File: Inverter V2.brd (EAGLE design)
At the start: 194.6 x 115.3 mm, 30 parts, among them Q1 ROHM_SCT3022ALGC11ROHM_SCT302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, Q2 ROHM_SCT3022ALGC11ROHM_SCT302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, Q3 ROHM_SCT3022ALGC11ROHM_SCT302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, Q4 ROHM_SCT3022ALGC11ROHM_SCT302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, Q5 ROHM_SCT3022ALGC11ROHM_SCT302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, Q6 ROHM_SCT3022ALGC11ROHM_SCT302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, U1 RASPBERRY_PICOTH

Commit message: Routing Inverter V2
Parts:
- added A0, A1: (no value), microbuilder:SOLDERJUMPER_REFLOW_NOPASTE
- added C4: 0.1µF, microbuilder:0603-NO
- added R12: 10K, microbuilder:RESPACK_4X0603
- added U2: INA219BIDCNT, microbuilder:SOT23-8
- SHUNT: device SparkFun-Connectors:1X02_2.54_SCREWTERM -> SparkFun-Connectors:1X02_XTRA_BIG
- VOUT: device SparkFun-Connectors:SCREWTERMINAL-3.5MM-3_LOCK.007S -> SparkFun-Connectors:SCREWTERMINAL-3.5MM-3-NS
- moved R8 127.0 mm to (31.3, 49.8), turned to 270 degrees
- moved R10 76.4 mm to (82.1, 53.6)
- moved R7 75.8 mm to (82.7, 76.3)
- moved R1 55.0 mm to (143.9, 20.1), turned to 90 degrees
- moved R6 23.6 mm to (62.6, 78.5)
- moved R11 16.9 mm to (66.2, 38.6)
- moved SHUNT 12.8 mm to (178.0, 52.5), turned to 90 degrees
- moved R9 12.1 mm to (68.4, 66.5)
- moved V+ 11.2 mm to (120.8, 16.1)
- moved C3 8.69 mm to (37.2, 56.3), turned to 180 degrees
- moved VOUT 7.08 mm to (188.3, 67.6)
- moved C7 7.01 mm to (57.7, 56.2)
- moved C6 6.98 mm to (53.3, 57.5)
- moved Q2 4.61 mm to (82.5, 64.9)
- moved Q6 4.61 mm to (164.0, 42.0)
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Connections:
- net N$1 renamed HIN1
- net N$10 renamed VGIN3
- net N$11 renamed VGIN2
- net N$12 renamed HO3
- net N$14 renamed VGIN6
- net N$16 renamed VGIN4
- net N$2 renamed LO1
- net N$3 renamed LIN1
- net N$5 renamed LIN2
- net N$6 renamed VGIN1
- net N$7 renamed HIN3
- net N$8 renamed VGIN5
- net N$9 renamed LIN3
- removed net VBUS: U1.40
- new net ADDR0: A0.2, R12.5, U2.7
- new net ADDR1: A1.2, R12.6, U2.8
- new net SCL: U1.2, U2.5
- new net SDA: U1.1, U2.6
- new net VCC: A0.1, A1.1, C4.1, U1.40, U2.4
- net GND1: now also C4.2, R12.3, R12.4, SHUNT.1, U2.2, U2.3; no longer SHUNT.P1
- net SHUNT: now also SHUNT.2, U2.1; no longer SHUNT.P2
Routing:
- net SHUNT: track 0.00 -> 246.4 mm
- net VOUT3/VS3: track 0.00 -> 189.3 mm
- net VS1/VOUT1: track 0.00 -> 166.3 mm
- net V+: track 0.00 -> 153.6 mm, vias 0 -> 2
- net VS2/VOUT2: track 0.00 -> 144.2 mm, vias 0 -> 2
- net VGIN6: track 0.00 -> 142.9 mm
- net VCC: track 0.00 -> 106.4 mm
- net VGIN5: track 0.00 -> 83.6 mm
- net VGIN4: track 0.00 -> 83.2 mm
- net SDA: track 0.00 -> 80.6 mm
- net VDD: track 0.00 -> 80.0 mm, vias 0 -> 2
- net SCL: track 0.00 -> 72.1 mm
- net VB3: track 0.00 -> 56.9 mm, vias 0 -> 2
- net LO1: track 0.00 -> 36.7 mm
- net LO2: track 0.00 -> 35.7 mm
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- added copper zone on layer 1, net GND1
- removed copper zone on layer 16, net GND1
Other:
- board size 194.6 x 115.3 mm -> 193.8 x 114 mm

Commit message: Revision to routed V2 inverter
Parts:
- C7: device rcl:SMC_Z -> rcl:E5-5
- moved C7 73.1 mm to (122.0, 21.5), turned to 0 degrees
- moved R11 18.5 mm to (51.7, 50.1), turned to 315 degrees
- moved R9 1.12 mm to (69.5, 66.5), turned to 45 degrees
- moved R6 0.90 mm to (63.4, 78.2), turned to 45 degrees
- moved C6 0.84 mm to (54.1, 57.5), turned to 315 degrees
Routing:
- net V+: track 153.6 -> 131.9 mm, vias 2 -> 0
- net HO3: track 34.9 -> 15.6 mm
- net VCC: track 106.4 -> 123.2 mm, vias 0 -> 2
- net VGIN3: track 19.0 -> 30.9 mm
- net GND1: track 1.25 -> 7.87 mm, vias 0 -> 2
- net VGIN1: track 27.0 -> 24.7 mm, vias 2 -> 1
- net VGIN2: track 14.7 -> 13.5 mm
- net HO1: track 18.3 -> 17.5 mm
- net N$15: track 4.21 -> 3.55 mm

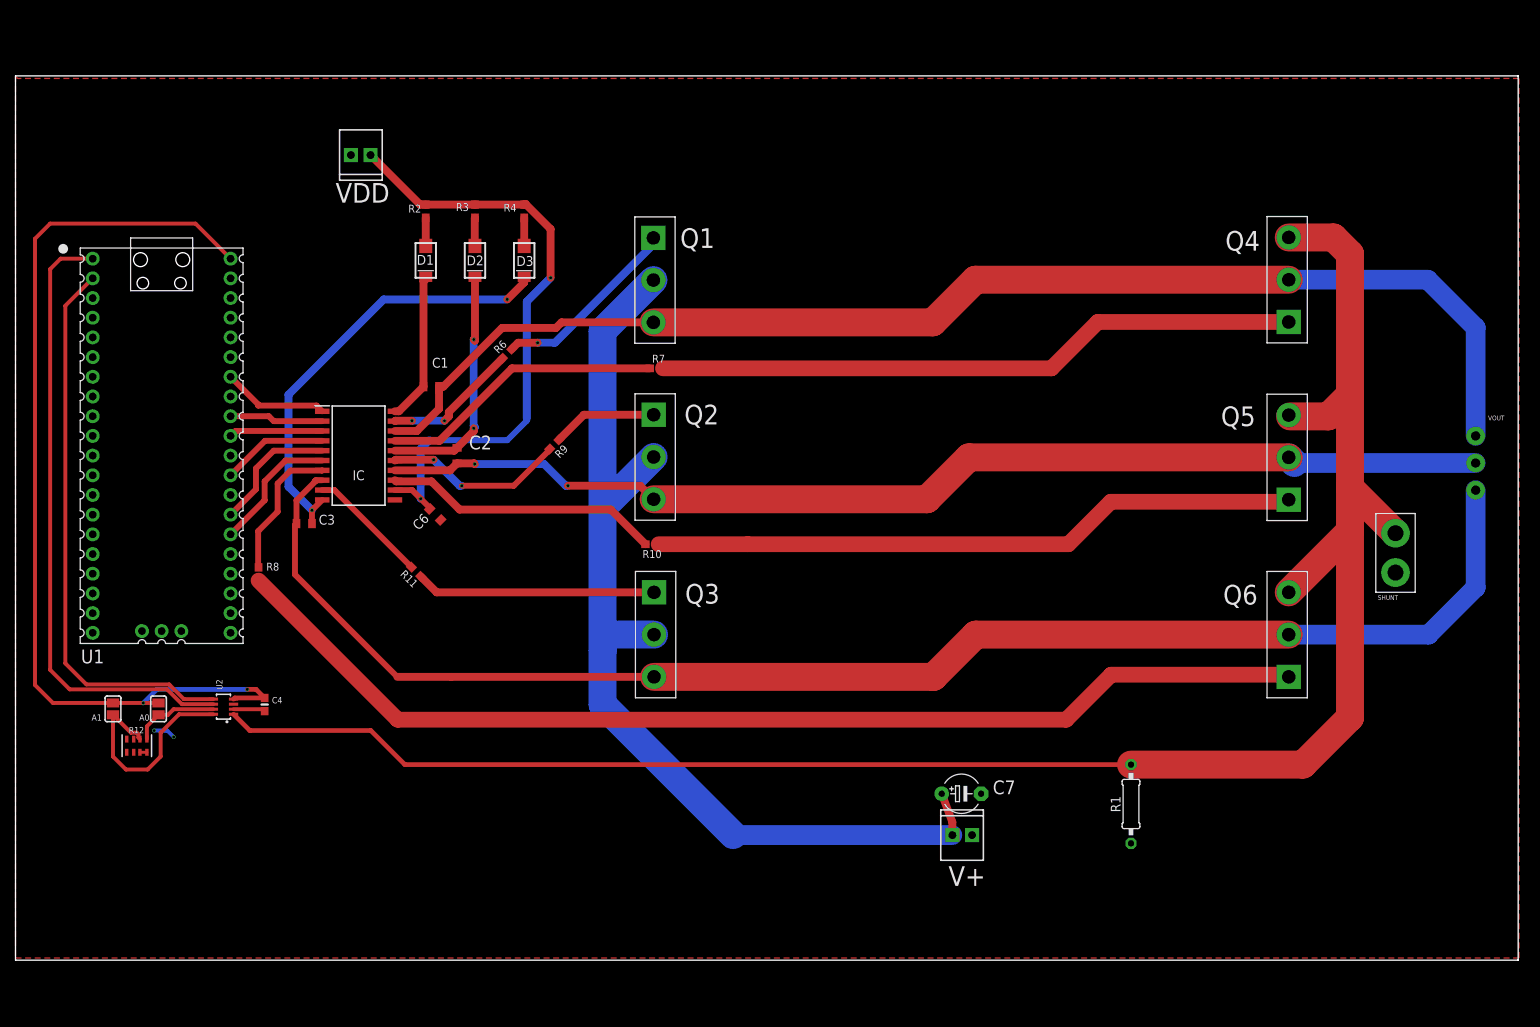
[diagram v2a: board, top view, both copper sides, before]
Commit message: Adjusted trace width + silkscreen
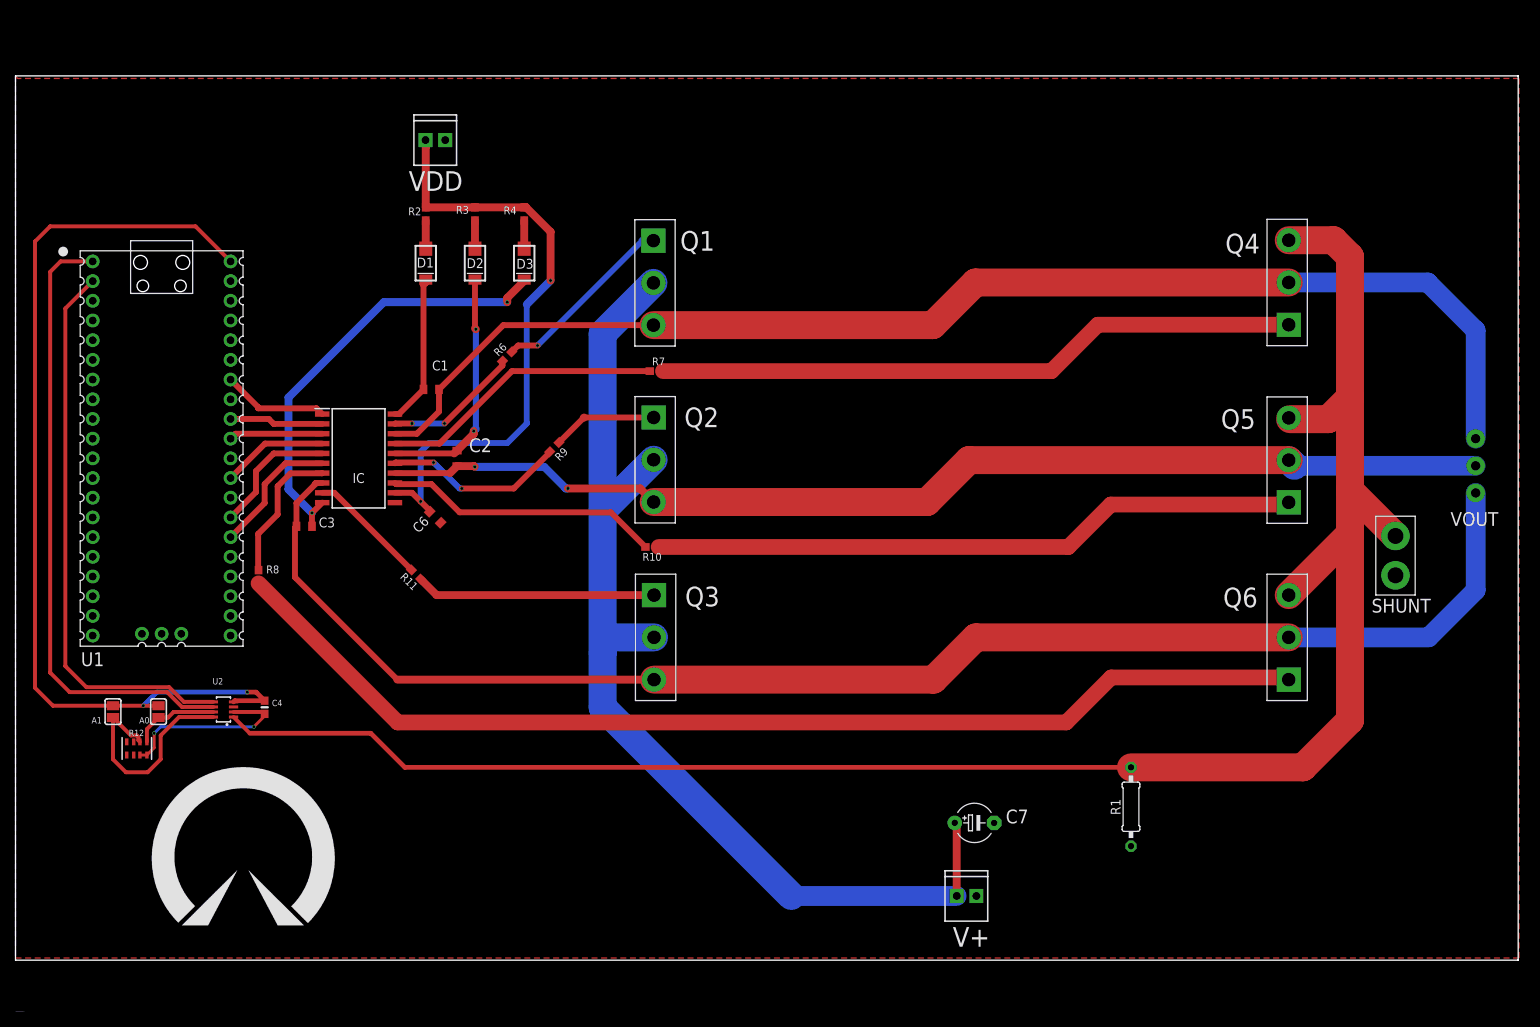
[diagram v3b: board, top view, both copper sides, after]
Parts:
- moved V+ 7.87 mm to (121.4, 8.28)
- moved VDD 7.34 mm to (52.9, 105.8), turned to 0 degrees
- moved C7 4.12 mm to (123.7, 17.7)
- moved Q4 0.36 mm to (164.0, 87.4)
- moved R6 0.36 mm to (63.4, 77.9)
- moved U1 0.36 mm to (18.8, 66.0)
- moved A0 0.36 mm to (18.4, 32.1)
- moved A1 0.36 mm to (12.6, 32.1)
- moved C4 0.36 mm to (32.1, 32.6)
- moved C6 0.36 mm to (54.1, 57.1)
- moved R11 0.36 mm to (51.7, 49.7)
- moved SHUNT 0.36 mm to (178.0, 52.2)
- moved R1 0.36 mm to (143.9, 19.8)
- moved R12 0.36 mm to (15.6, 27.3)
- moved C1 0.36 mm to (53.6, 73.6)
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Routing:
- net GND1: track 7.87 -> 23.6 mm
- net V+: track 131.9 -> 139.5 mm
- net VDD: track 80.4 -> 79.3 mm
- net VS1/VOUT1: track 166.3 -> 165.7 mm
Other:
- board text added: "C:/Users/leapa/Desktop/hx logo.bmp"
